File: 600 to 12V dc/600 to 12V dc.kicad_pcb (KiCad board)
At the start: 2 copper layers, 66.8 x 60 mm, 40 parts, among them J1 Conn_01x02_Pin, J2 Conn_01x02_Pin, J3 Conn_01x02_Pin, Q1 TK3P80E, U2 LT8316EFE-PBF

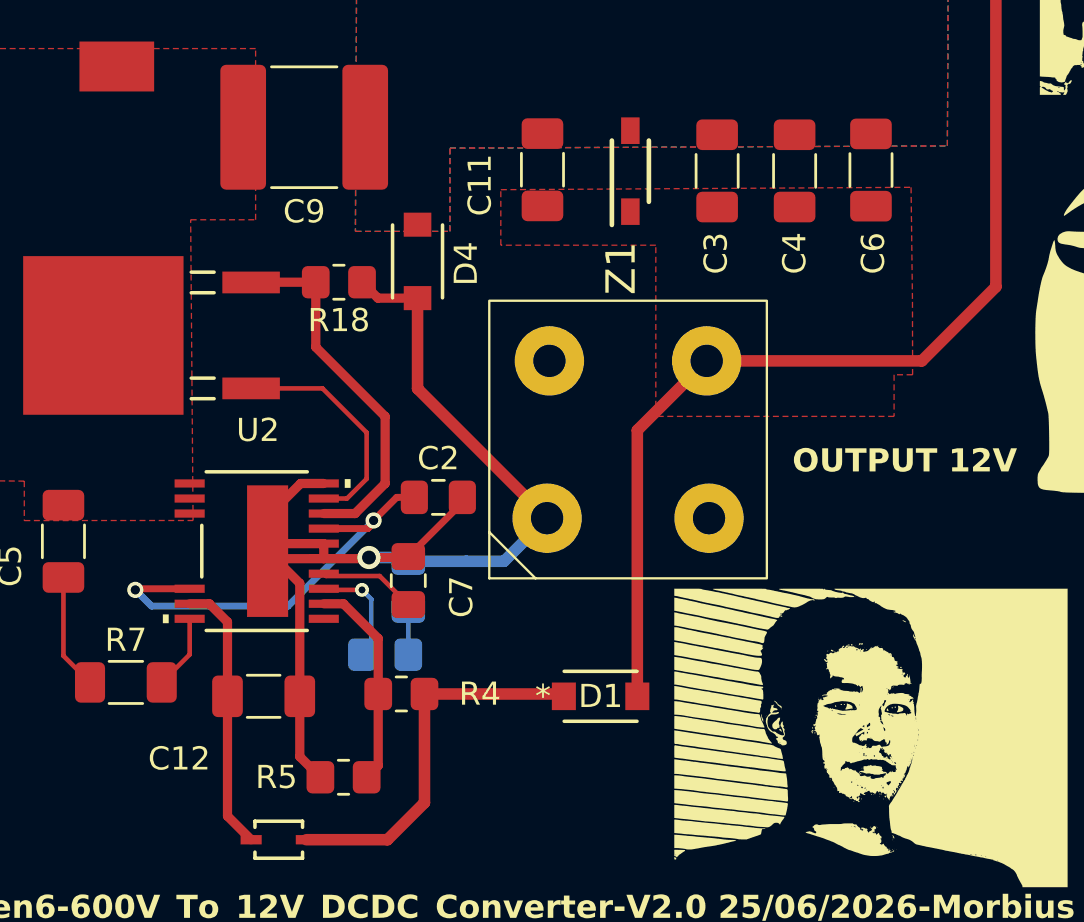
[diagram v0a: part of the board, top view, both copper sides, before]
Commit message: TSAL GREEN SYSTEM V2 READY TO FAB
SCH&PCB updated for both HVB V2 and ACCUM V2

PCB is 9 draw at work btw
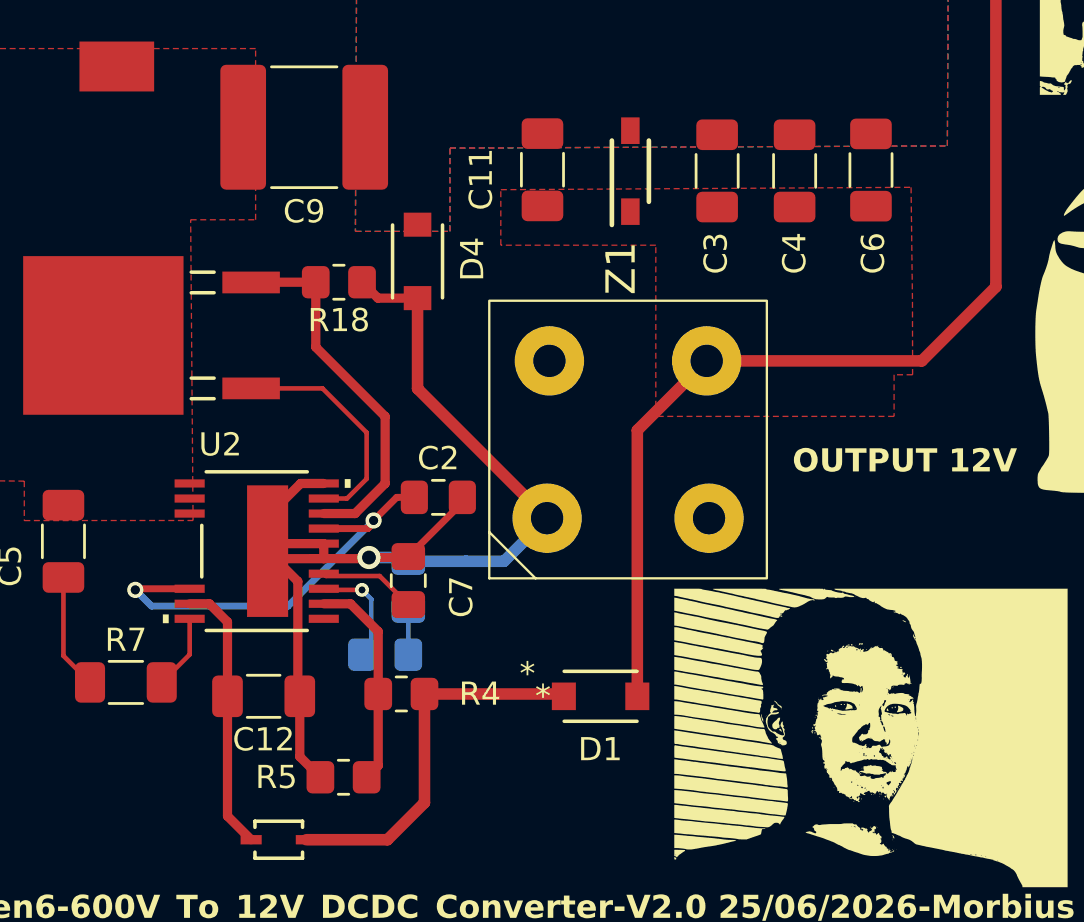
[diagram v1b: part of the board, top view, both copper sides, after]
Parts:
- moved G*** 18.2 mm to (126.6, 93.6)
- moved G*** 15.8 mm to (135.4, 127.3)
- moved G*** 6.41 mm to (143.6, 100.6)
